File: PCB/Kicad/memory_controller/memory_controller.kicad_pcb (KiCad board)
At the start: 6 copper layers, 180 x 100 mm, 116 parts, among them U1 74245, U10 74283, U11 74377, U12 74377, U13 74245, U14 74245, U15 74245, U16 74245, U17 74245, U18 74245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

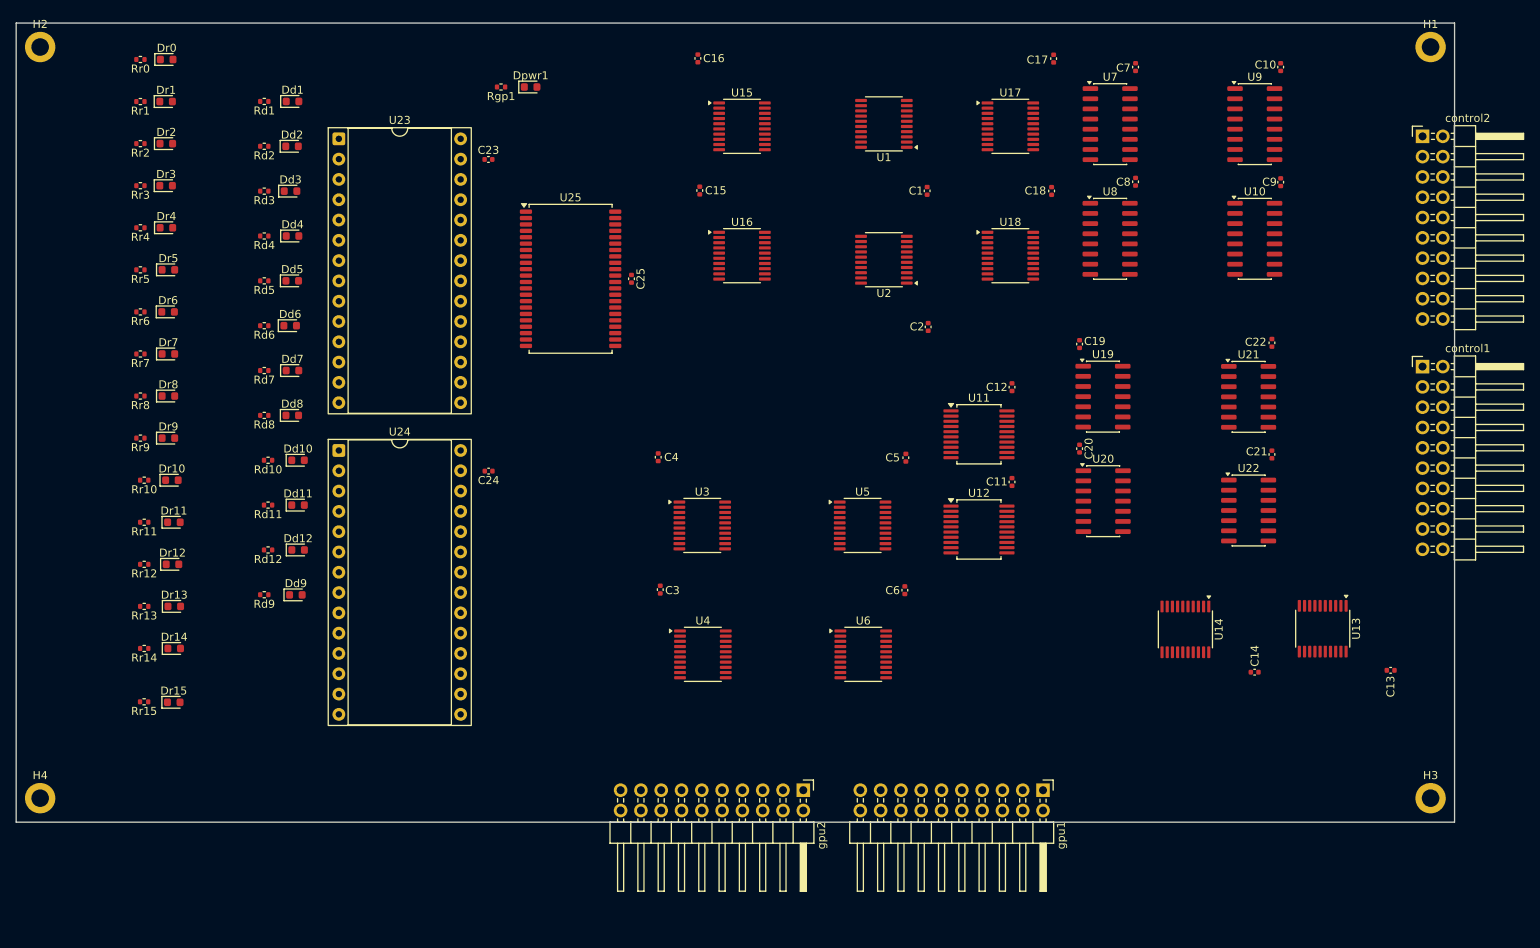
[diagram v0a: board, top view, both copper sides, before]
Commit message: routed control signals
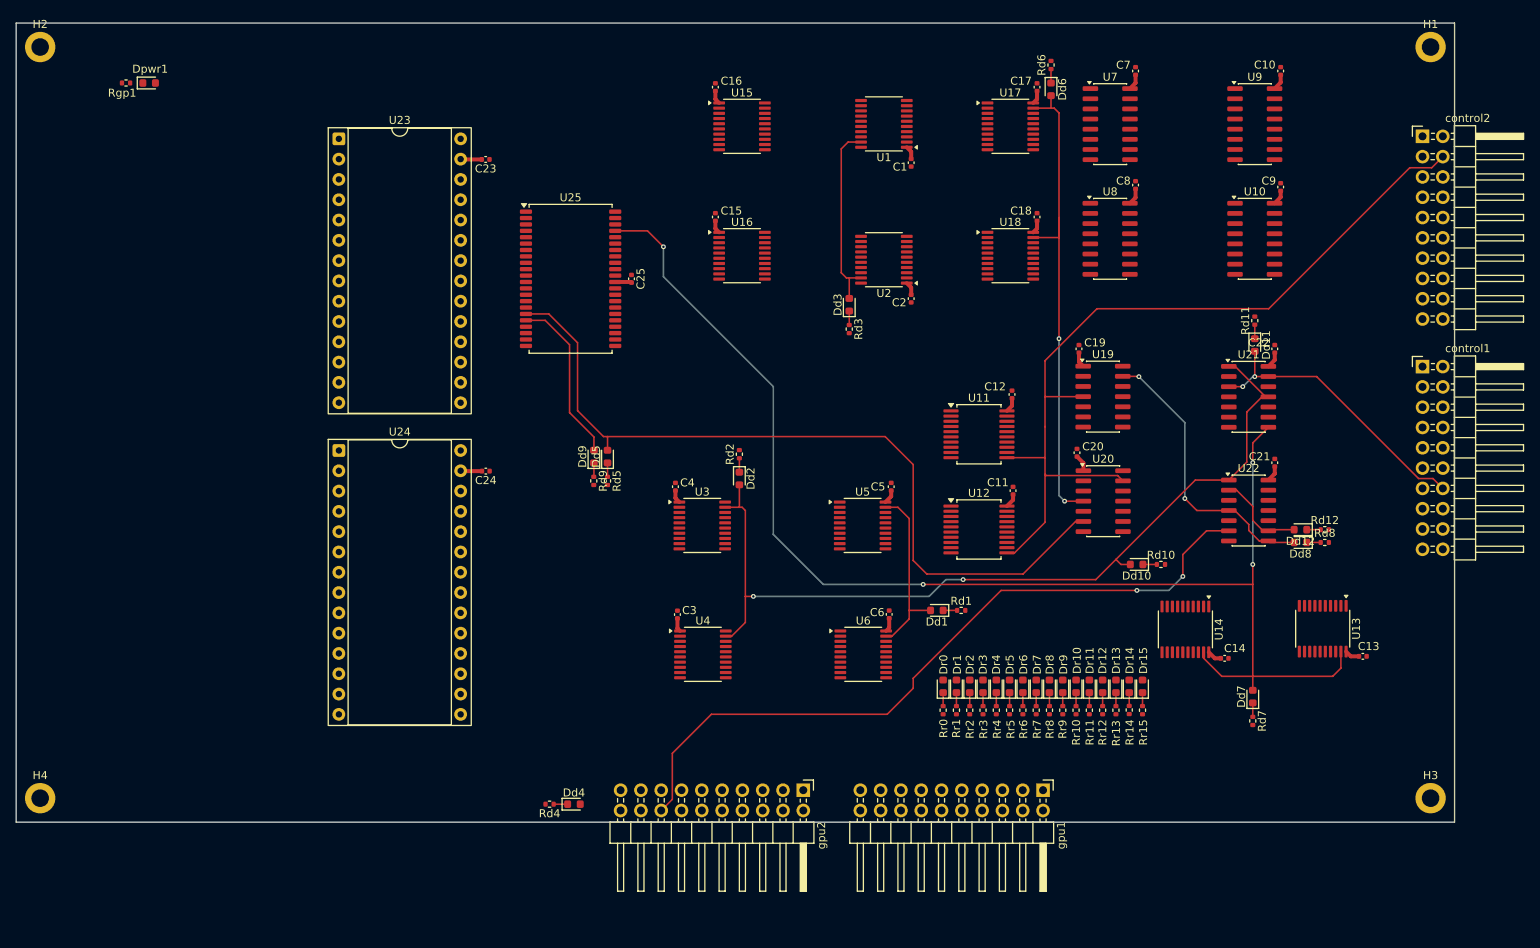
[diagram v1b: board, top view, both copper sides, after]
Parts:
- moved Rd8 133.7 mm to (263.8, 135.0), turned to 0 degrees
- moved Rd12 132.3 mm to (263.8, 133.4), turned to 0 degrees
- moved Rd7 131.2 mm to (254.8, 157.3), turned to -90 degrees
- moved Rr0 129.3 mm to (216.0, 156.0), turned to -90 degrees
- moved Rr1 127.4 mm to (217.7, 156.0), turned to -90 degrees
- moved Dd8 127.2 mm to (260.7, 135.0), turned to 180 degrees
- moved Dd7 126.9 mm to (254.8, 154.3), turned to 90 degrees
- moved Rr2 125.7 mm to (219.3, 156.0), turned to -90 degrees
- moved Rd11 125.6 mm to (255.0, 107.2), turned to 90 degrees
- moved Dd12 125.5 mm to (260.7, 133.4), turned to 180 degrees
- moved Rr15 124.9 mm to (240.9, 156.0), turned to -90 degrees
- moved Dr0 124.9 mm to (216.0, 153.0), turned to 90 degrees
- moved Rr3 124.2 mm to (221.0, 156.0), turned to -90 degrees
- moved Rr14 123.5 mm to (239.3, 156.0), turned to -90 degrees
- moved Dr1 123.0 mm to (217.7, 153.0), turned to 90 degrees
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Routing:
- net /~{OUTPUT_ENABLE}: track 0.00 -> 166.2 mm, vias 0 -> 4
- net /~{OE}_n: track 0.00 -> 110.7 mm, vias 0 -> 2
- net /CLK: track 0.00 -> 106.6 mm
- net /~{WE}_mem: track 0.00 -> 99.7 mm
- net /GPU_WE: track 0.00 -> 91.2 mm, vias 0 -> 2
- net /~{OE}_MUX_n: track 0.00 -> 62.0 mm, vias 0 -> 2
- net VCC: track 0.00 -> 47.7 mm
- net /MODE1: track 0.00 -> 36.3 mm, vias 0 -> 2
- net /WRITE_ENABLE: track 0.00 -> 36.1 mm, vias 0 -> 2
- net /OUTPUT_ENABLE: track 0.00 -> 23.6 mm
- net /~{OE}_p: track 0.00 -> 22.6 mm
- net /GPU_ADDR15: track 0.00 -> 21.2 mm
- net /MODE2: track 0.00 -> 11.4 mm
- net Net-(Dd9-K): track 0.00 -> 1.76 mm
- net Net-(Dd8-K): track 0.00 -> 1.75 mm
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
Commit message: bus start
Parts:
- moved Rd3 35.1 mm to (212.5, 74.2), turned to 90 degrees
- moved Dd3 29.2 mm to (212.5, 77.2), turned to -90 degrees
- moved C2 27.4 mm to (204.7, 78.0), turned to -90 degrees
- moved U1 17.3 mm to (208.1, 99.9), turned to 0 degrees
- moved U2 16.7 mm to (208.1, 82.9), turned to 0 degrees
- moved C1 10.5 mm to (204.7, 95.0), turned to -90 degrees
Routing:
- net /OUTPUT_ENABLE: track 23.6 -> 4.05 mm
- net /RegAddr/DATA_IN1: track 0.00 -> 14.7 mm, vias 0 -> 2
- net /RegAddr/DATA_IN9: track 0.00 -> 14.7 mm, vias 0 -> 2
- net /RegAddr/DATA_IN11: track 0.00 -> 14.6 mm, vias 0 -> 2
- net /RegAddr/DATA_IN3: track 0.00 -> 14.6 mm, vias 0 -> 2
- net /RegAddr/DATA_IN5: track 0.00 -> 14.6 mm, vias 0 -> 2
- net /RegAddr/DATA_IN13: track 0.00 -> 14.6 mm, vias 0 -> 2
- net /RegAddr/DATA_IN8: track 0.00 -> 14.6 mm, vias 0 -> 2
- net /RegAddr/DATA_IN0: track 0.00 -> 14.6 mm, vias 0 -> 2
- net /RegAddr/DATA_IN12: track 0.00 -> 14.6 mm, vias 0 -> 2
- net /RegAddr/DATA_IN7: track 0.00 -> 14.6 mm, vias 0 -> 2
- net /RegAddr/DATA_IN4: track 0.00 -> 14.6 mm, vias 0 -> 2
- net /RegAddr/DATA_IN2: track 0.00 -> 14.6 mm, vias 0 -> 2
- net /RegAddr/DATA_IN14: track 0.00 -> 14.6 mm, vias 0 -> 2
- net /RegAddr/DATA_IN6: track 0.00 -> 14.6 mm, vias 0 -> 2
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
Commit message: bus in progress
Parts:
- control2: value ~ -> out
- moved C2 75.2 mm to (168.4, 143.9)
- moved U2 75.2 mm to (171.8, 148.8)
- moved C1 49.9 mm to (168.5, 129.3)
- moved U1 49.9 mm to (171.9, 134.2)
- moved Dd3 43.4 mm to (198.5, 118.3)
- moved Rd3 43.4 mm to (198.5, 115.2)
- moved C24 8.70 mm to (150.1, 125.8)
- moved C23 8.70 mm to (150.1, 86.8)
- moved U23 8.70 mm to (131.7, 84.2)
- moved U24 8.70 mm to (131.7, 123.2)
- moved Rd1 3.62 mm to (214.6, 143.5), turned to 180 degrees
- moved Rd10 3.62 mm to (239.6, 137.8), turned to 180 degrees
- moved Rd7 3.62 mm to (254.8, 153.7), turned to 90 degrees
- moved Rd6 3.60 mm to (229.5, 78.8), turned to -90 degrees
- moved Rd2 3.59 mm to (190.5, 127.5), turned to -90 degrees
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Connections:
- Dd1 pad 2: /~{OE}_p -> VCC
- Dd10 pad 2: /~{OE}_n -> VCC
- Dd2 pad 2: /~{OE}_n -> VCC
- Dd5 pad 2: /~{WE}_mem -> VCC
- Dd6 pad 2: /~{OE}_MUX_n -> VCC
- Dd7 pad 2: /~{OUTPUT_ENABLE} -> VCC
- Rd1 pad 2: GND -> /~{OE}_p
- Rd10 pad 2: GND -> /~{OE}_n
- Rd2 pad 2: GND -> /~{OE}_n
- Rd5 pad 2: GND -> /~{WE}_mem
- Rd6 pad 2: GND -> /~{OE}_MUX_n
- Rd7 pad 2: GND -> /~{OUTPUT_ENABLE}
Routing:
- net /GPU_ADDR7: track 0.00 -> 100.4 mm, vias 0 -> 2
- net /GPU_ADDR6: track 0.00 -> 98.0 mm, vias 0 -> 2
- net /GPU_ADDR5: track 0.00 -> 95.1 mm, vias 0 -> 2
- net /DATA_BUS15: track 0.00 -> 92.1 mm, vias 0 -> 4
- net /GPU_ADDR8: track 0.00 -> 90.9 mm, vias 0 -> 4
- net /GPU_ADDR9: track 0.00 -> 88.1 mm, vias 0 -> 5
- net /GPU_ADDR11: track 0.00 -> 83.5 mm, vias 0 -> 5
- net /GPU_ADDR4: track 0.00 -> 81.7 mm, vias 0 -> 2
- net /GPU_ADDR3: track 0.00 -> 81.0 mm, vias 0 -> 2
- net /GPU_ADDR2: track 0.00 -> 80.6 mm, vias 0 -> 2
- net /GPU_ADDR1: track 0.00 -> 80.1 mm, vias 0 -> 2
- net /GPU_ADDR0: track 0.00 -> 79.8 mm, vias 0 -> 2
- net /GPU_ADDR10: track 0.00 -> 78.9 mm, vias 0 -> 3
- net /GPU_ADDR12: track 0.00 -> 43.6 mm, vias 0 -> 3
- net /GPU_ADDR14: track 0.00 -> 42.8 mm, vias 0 -> 3
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
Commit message: continuing bus routing
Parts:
- moved Dd4 89.4 mm to (118.3, 94.7)
- moved Rd4 89.4 mm to (115.2, 94.7)
- moved Dd3 86.5 mm to (117.7, 87.6)
- moved Rd3 86.5 mm to (117.7, 84.5)
- moved Dr0 67.8 mm to (278.8, 178.3), turned to -90 degrees
- moved C9 67.4 mm to (233.6, 153.2), turned to 180 degrees
- moved U10 66.2 mm to (228.6, 157.7)
- moved Rr0 65.8 mm to (278.8, 175.3), turned to 90 degrees
- moved C10 65.6 mm to (200.4, 106.9)
- moved U9 65.6 mm to (197.1, 113.6)
- moved Dr1 64.7 mm to (277.2, 178.3), turned to -90 degrees
- moved Rr1 62.6 mm to (277.2, 175.3), turned to 90 degrees
- moved Dr2 61.6 mm to (275.5, 178.3), turned to -90 degrees
- moved Rr2 59.4 mm to (275.5, 175.3), turned to 90 degrees
- moved Dr3 58.6 mm to (273.9, 178.3), turned to -90 degrees
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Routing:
- net /output_MUX/DATA_OUT0: track 24.5 -> 128.5 mm, vias 2 -> 4
- net /DATA_BUS15: track 92.1 -> 4.51 mm, vias 4 -> 2
- net /GPU_ADDR1: track 80.1 -> 163.2 mm, vias 2 -> 6
- net /GPU_ADDR0: track 79.8 -> 151.9 mm, vias 2 -> 6
- net /GPU_ADDR5: track 95.1 -> 164.9 mm, vias 2 -> 8
- net /GPU_DATA12: track 13.0 -> 70.1 mm, vias 2 -> 5
- net /GPU_DATA13: track 12.4 -> 69.5 mm, vias 2 -> 5
- net /GPU_DATA14: track 13.0 -> 69.0 mm, vias 2 -> 5
- net Net-(U8-CIN): track 0.00 -> 56.0 mm, vias 0 -> 4
- net /GPU_DATA15: track 12.4 -> 68.0 mm, vias 2 -> 5
- net /GPU_DATA8: track 12.9 -> 67.6 mm, vias 2 -> 3
- net /GPU_DATA9: track 12.4 -> 65.7 mm
- net /GPU_DATA10: track 13.0 -> 65.1 mm, vias 2 -> 3
- net /GPU_DATA11: track 14.5 -> 64.7 mm
- net /GPU_DATA0: track 10.9 -> 55.5 mm, vias 1 -> 4
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
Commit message: continuing bus routing
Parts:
- moved Dr0 80.9 mm to (258.1, 100.1)
- moved Dr1 80.9 mm to (256.4, 100.1)
- moved Dr11 80.9 mm to (239.8, 100.1)
- moved Dr12 80.9 mm to (238.1, 100.1)
- moved Dr13 80.9 mm to (236.5, 100.1)
- moved Dr14 80.9 mm to (234.8, 100.1)
- moved Dr15 80.9 mm to (233.1, 100.1)
- moved Dr3 80.9 mm to (253.1, 100.1)
- moved Dr4 80.9 mm to (251.4, 100.1)
- moved Dr6 80.9 mm to (248.1, 100.1)
- moved Dr8 80.9 mm to (244.8, 100.1)
- moved Dr9 80.9 mm to (243.1, 100.1)
- moved Rr0 80.9 mm to (258.1, 97.1)
- moved Rr1 80.9 mm to (256.4, 97.1)
- moved Rr11 80.9 mm to (239.8, 97.1)
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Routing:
- net /GPU_DATA6: track 51.1 -> 197.2 mm, vias 4 -> 7
- net /GPU_DATA7: track 51.0 -> 197.0 mm, vias 4 -> 7
- net /GPU_DATA5: track 51.2 -> 192.8 mm, vias 4 -> 9
- net /GPU_DATA4: track 51.5 -> 191.6 mm, vias 4 -> 8
- net /GPU_DATA3: track 54.1 -> 186.4 mm, vias 4 -> 8
- net /GPU_DATA2: track 54.6 -> 182.7 mm, vias 4 -> 8
- net /GPU_DATA1: track 55.2 -> 170.5 mm, vias 4 -> 6
- net /GPU_DATA0: track 55.5 -> 169.5 mm, vias 4 -> 7
- net /output_MUX/DATA_OUT1: track 24.8 -> 128.4 mm, vias 2 -> 4
- net /output_MUX/DATA_OUT2: track 24.6 -> 126.2 mm, vias 2 -> 4
- net /output_MUX/DATA_OUT3: track 24.6 -> 125.8 mm, vias 2 -> 4
- net /output_MUX/DATA_OUT4: track 24.5 -> 123.7 mm, vias 2 -> 4
- net /output_MUX/DATA_OUT5: track 24.6 -> 123.3 mm, vias 2 -> 4
- net /output_MUX/DATA_OUT6: track 24.5 -> 121.3 mm, vias 2 -> 4
- net /output_MUX/DATA_OUT7: track 24.6 -> 120.9 mm, vias 2 -> 4
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
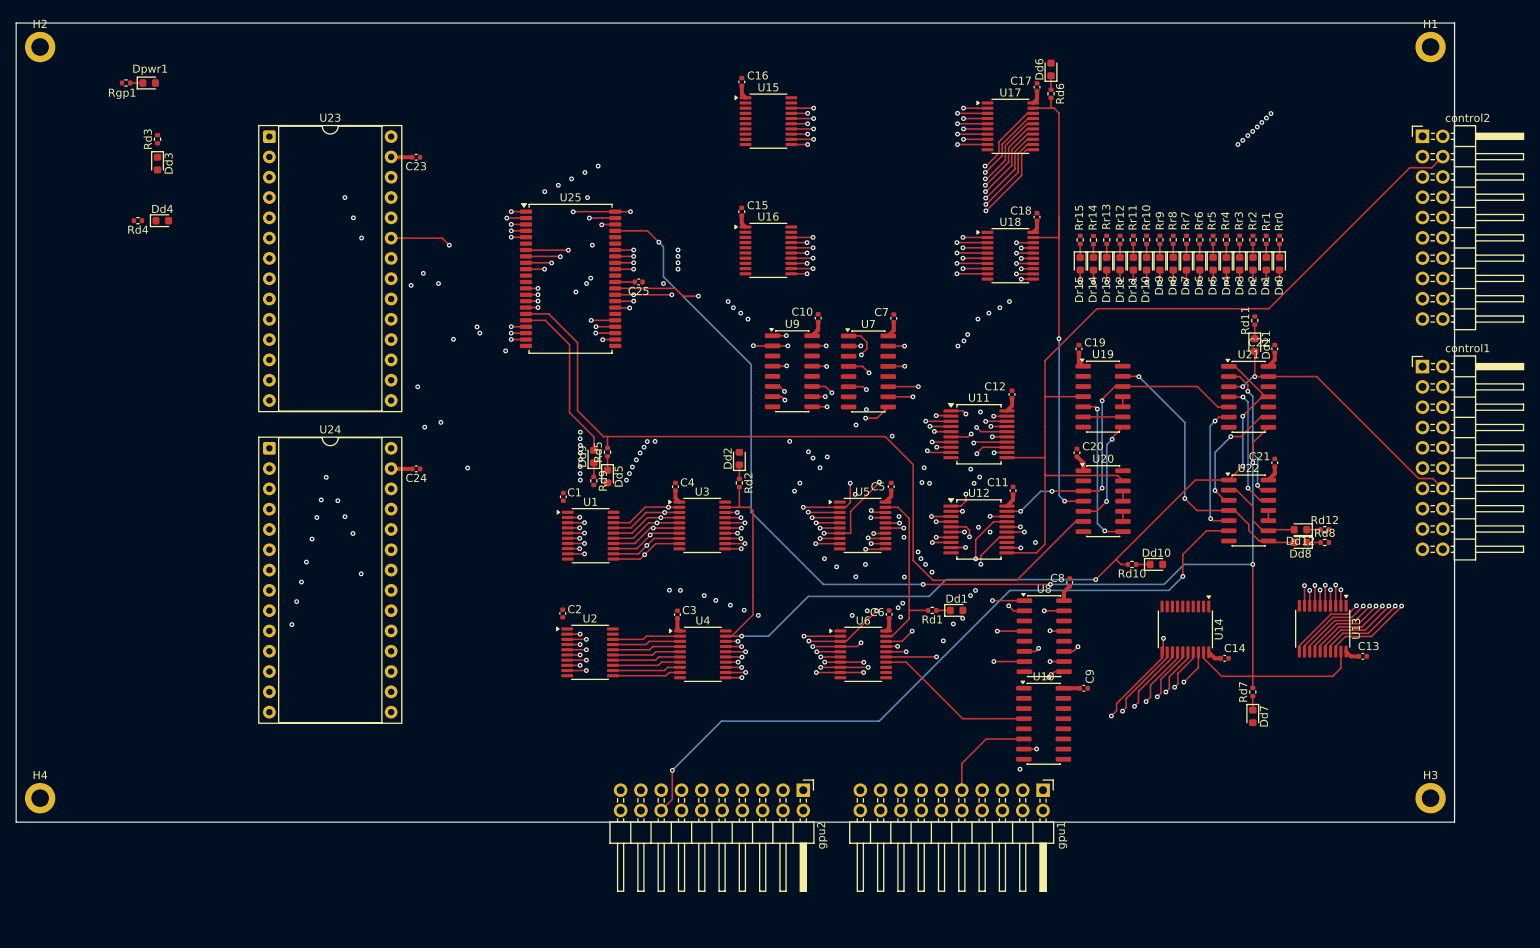
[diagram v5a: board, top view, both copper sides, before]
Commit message: routed signals and buses
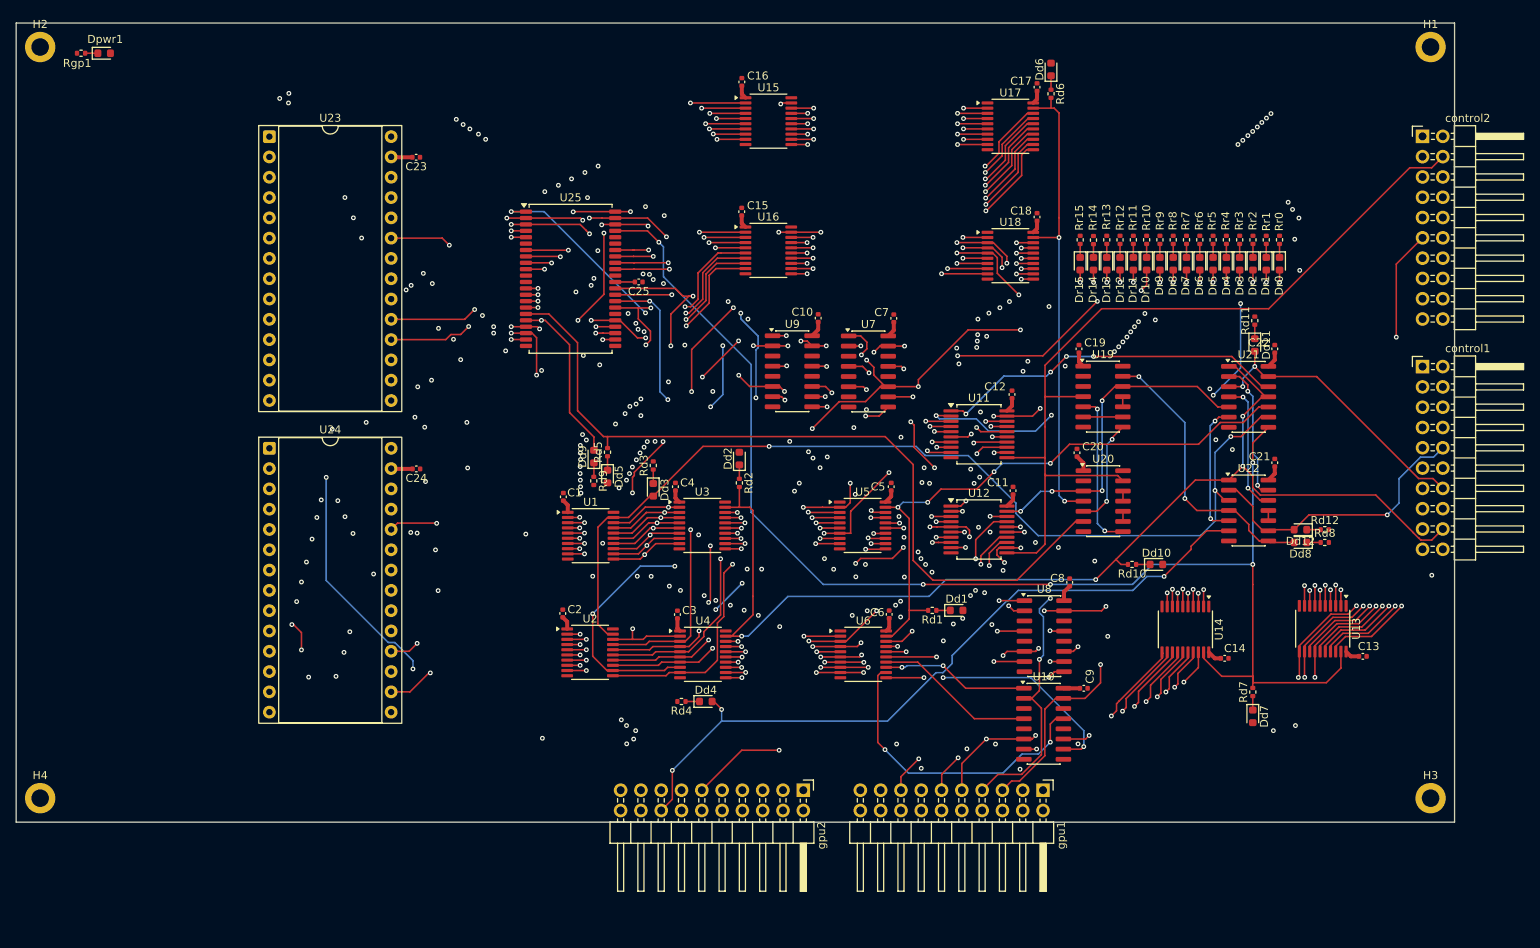
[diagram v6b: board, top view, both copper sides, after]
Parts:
- moved Dd4 90.8 mm to (186.3, 154.9)
- moved Rd4 90.8 mm to (183.3, 154.9)
- moved Dd3 74.3 mm to (179.7, 128.4)
- moved Rd3 74.3 mm to (179.7, 125.4)
- moved Dpwr1 6.75 mm to (111.0, 73.8)
- moved Rgp1 6.75 mm to (108.1, 73.8)
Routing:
- net /GPU_ADDR4: track 120.4 -> 299.6 mm, vias 6 -> 9
- net /GPU_ADDR3: track 97.9 -> 275.2 mm, vias 5 -> 12
- net /GPU_ADDR12: track 97.6 -> 268.0 mm, vias 5 -> 10
- net /GPU_ADDR2: track 105.2 -> 273.1 mm, vias 6 -> 10
- net /GPU_ADDR14: track 80.4 -> 241.4 mm, vias 5 -> 11
- net /GPU_ADDR9: track 106.9 -> 264.3 mm, vias 8 -> 23
- net /GPU_ADDR7: track 127.8 -> 280.4 mm, vias 5 -> 10
- net /GPU_ADDR8: track 118.0 -> 263.9 mm, vias 9 -> 16
- net /GPU_ADDR13: track 73.2 -> 216.6 mm, vias 5 -> 12
- net /GPU_ADDR6: track 134.2 -> 275.9 mm, vias 6 -> 10
- net /DATA_BUS3: track 32.0 -> 165.3 mm, vias 2 -> 3
- net /GPU_ADDR15: track 96.3 -> 226.9 mm, vias 5 -> 14
- net /GPU_ADDR10: track 134.9 -> 264.3 mm, vias 8 -> 13
- net /DATA_BUS2: track 28.8 -> 154.1 mm
- net /GPU_ADDR0: track 153.4 -> 278.1 mm, vias 7 -> 12
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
